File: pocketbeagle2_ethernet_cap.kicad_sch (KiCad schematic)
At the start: 1 part, among them U1 PocketBeagle2

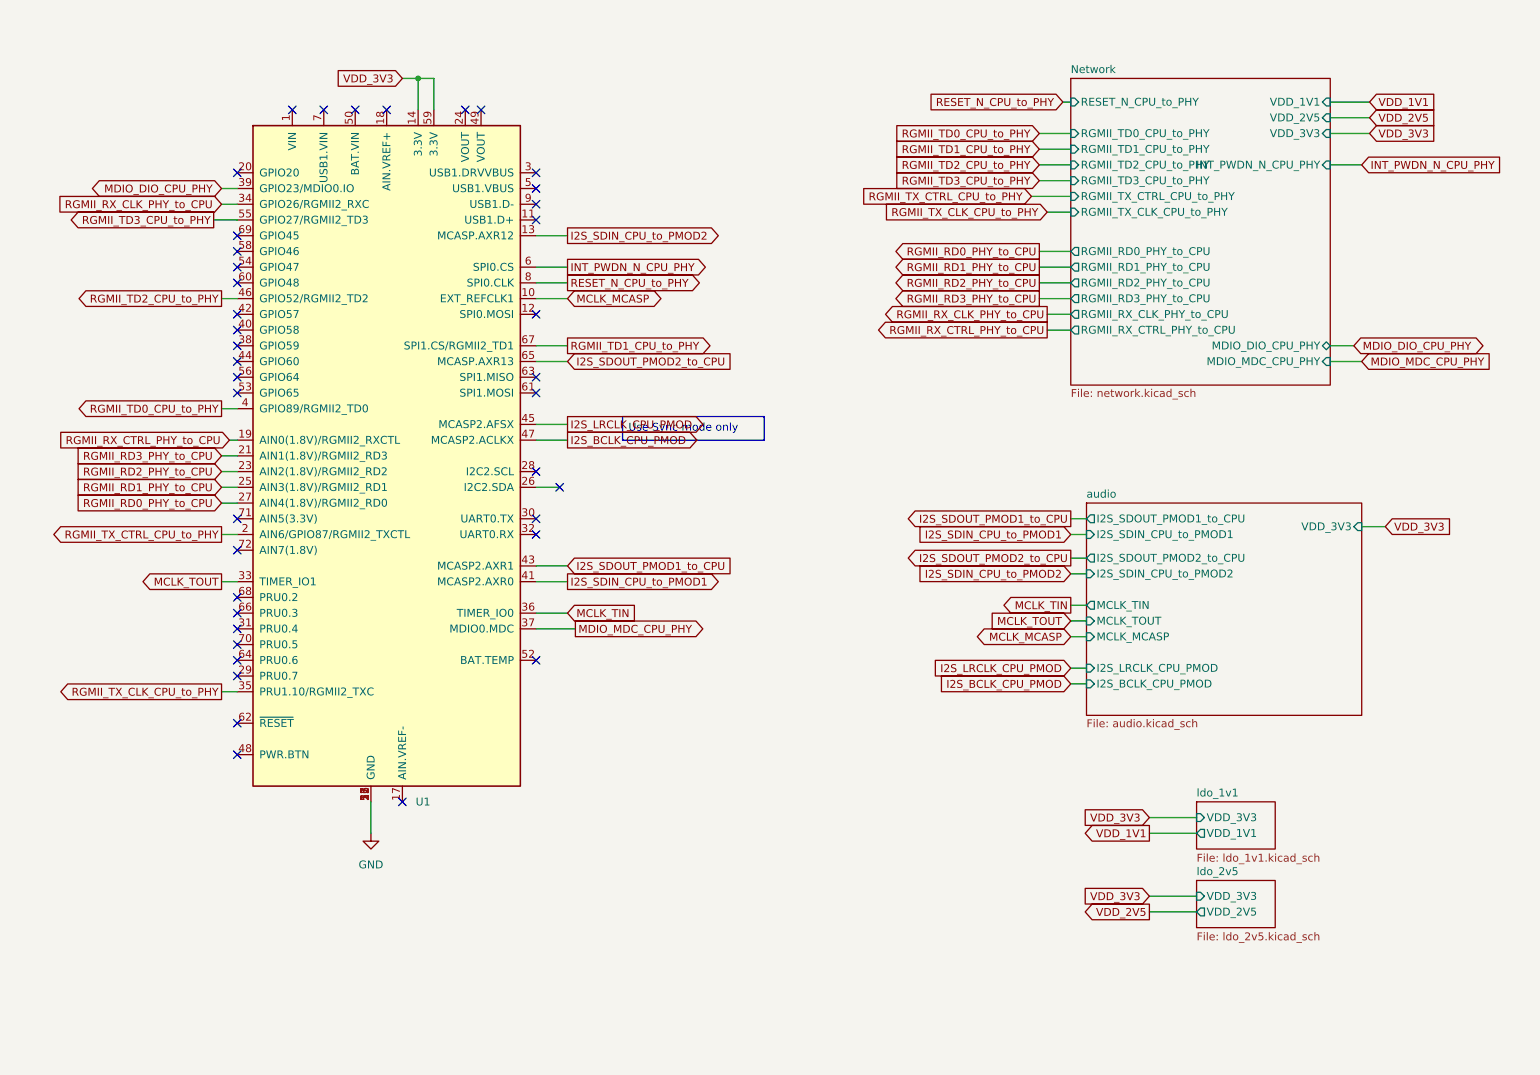
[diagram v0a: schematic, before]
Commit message: Replace audio PMOD sheet with full IO pass-through expansion headers
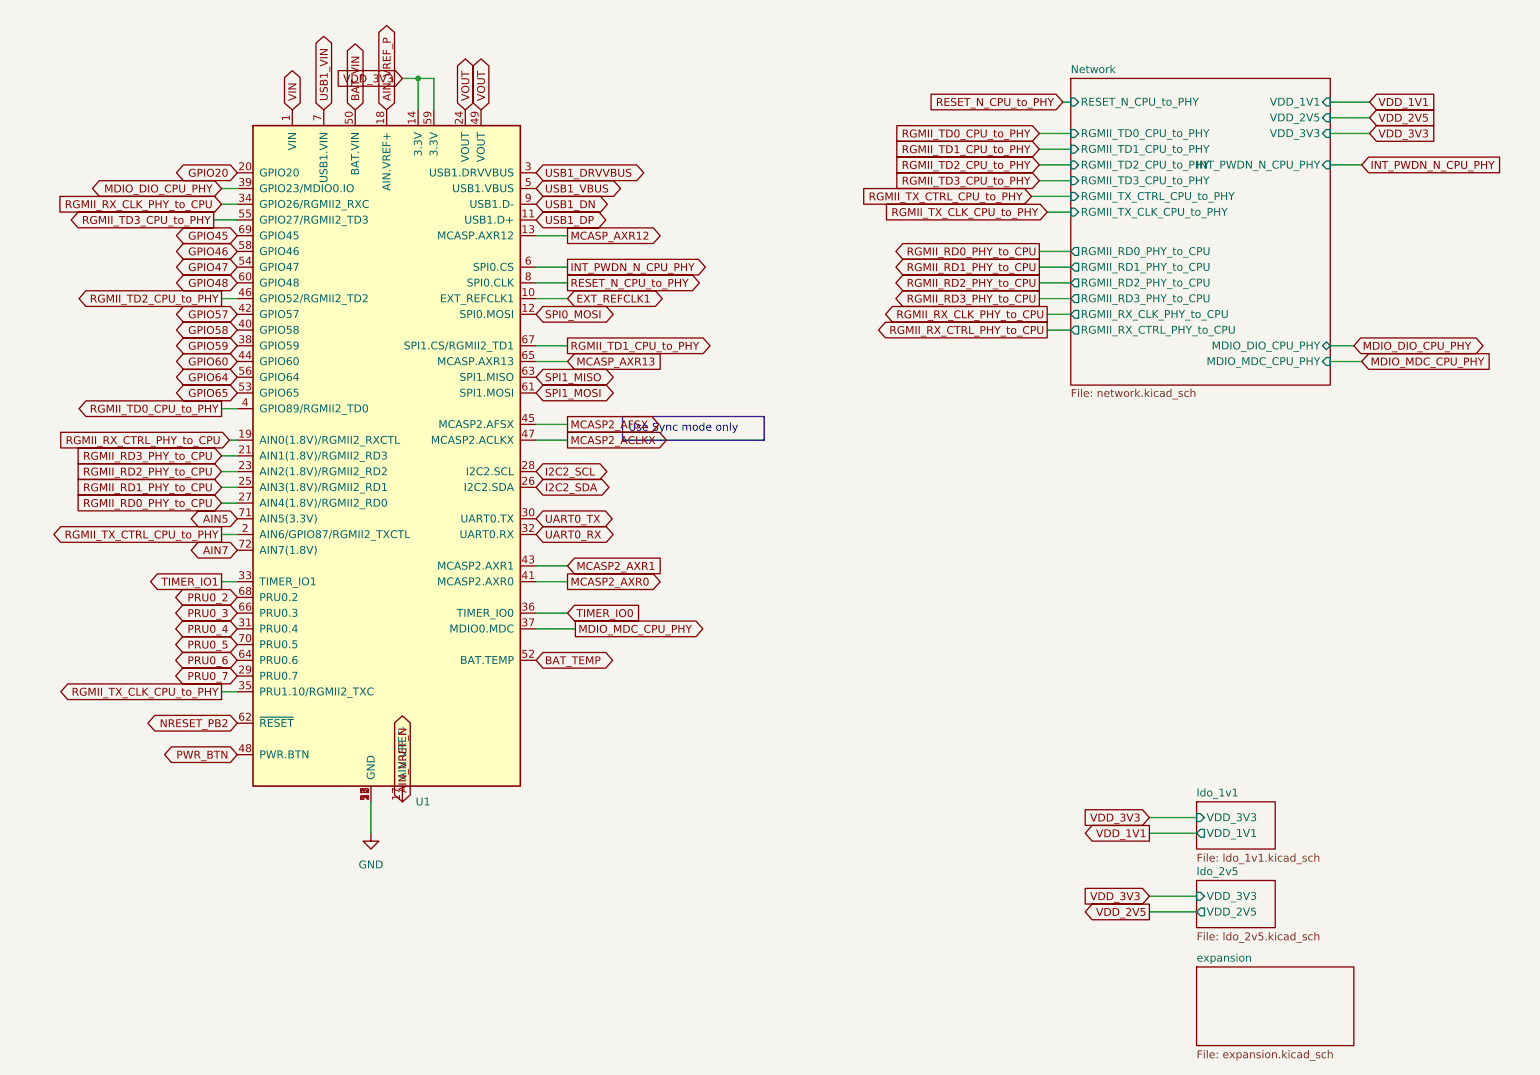
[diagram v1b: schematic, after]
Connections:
- net VIN: now reaches U1.1 (VIN)
- net USB1_DP: now reaches U1.11 (USB1.D+)
- net SPI0_MOSI: now reaches U1.12 (SPI0.MOSI)
- net AIN_VREF_N: now reaches U1.17 (AIN.VREF-)
- net AIN_VREF_P: now reaches U1.18 (AIN.VREF+)
- net GPIO20: now reaches U1.20 (GPIO20)
- net VOUT: now reaches U1.24 (VOUT)
- net VOUT: now also U1.49 (VOUT)
- net I2C2_SDA: now reaches U1.26 (I2C2.SDA)
- net I2C2_SCL: now reaches U1.28 (I2C2.SCL)
- net PRU0_7: now reaches U1.29 (PRU0.7)
- net USB1_DRVVBUS: now reaches U1.3 (USB1.DRVVBUS)
- net UART0_TX: now reaches U1.30 (UART0.TX)
- net PRU0_4: now reaches U1.31 (PRU0.4)
- net UART0_RX: now reaches U1.32 (UART0.RX)
- net GPIO59: now reaches U1.38 (GPIO59)
- net GPIO58: now reaches U1.40 (GPIO58)
- net GPIO57: now reaches U1.42 (GPIO57)
- net GPIO60: now reaches U1.44 (GPIO60)
- net PWR_BTN: now reaches U1.48 (PWR.BTN)
- net USB1_VBUS: now reaches U1.5 (USB1.VBUS)
- net BAT_VIN: now reaches U1.50 (BAT.VIN)
- net BAT_TEMP: now reaches U1.52 (BAT.TEMP)
- net GPIO65: now reaches U1.53 (GPIO65)
- net GPIO47: now reaches U1.54 (GPIO47)
- net GPIO64: now reaches U1.56 (GPIO64)
- net GPIO46: now reaches U1.58 (GPIO46)
- net GPIO48: now reaches U1.60 (GPIO48)
- net SPI1_MOSI: now reaches U1.61 (SPI1.MOSI)
- net NRESET_PB2: now reaches U1.62 (~{RESET})
- net SPI1_MISO: now reaches U1.63 (SPI1.MISO)
- net PRU0_6: now reaches U1.64 (PRU0.6)
- net PRU0_3: now reaches U1.66 (PRU0.3)
- net PRU0_2: now reaches U1.68 (PRU0.2)
- net GPIO45: now reaches U1.69 (GPIO45)
- net USB1_VIN: now reaches U1.7 (USB1.VIN)
- net PRU0_5: now reaches U1.70 (PRU0.5)
- net AIN5: now reaches U1.71 (AIN5(3.3V))
- net AIN7: now reaches U1.72 (AIN7(1.8V))
- net USB1_DN: now reaches U1.9 (USB1.D-)
- net I2S_BCLK_CPU_PMOD renamed MCASP2_ACLKX
- net I2S_LRCLK_CPU_PMOD renamed MCASP2_AFSX
- net I2S_SDIN_CPU_to_PMOD1 renamed MCASP2_AXR0
- net I2S_SDIN_CPU_to_PMOD2 renamed MCASP_AXR12
- net I2S_SDOUT_PMOD1_to_CPU renamed MCASP2_AXR1
- net I2S_SDOUT_PMOD2_to_CPU renamed MCASP_AXR13
- net MCLK_MCASP renamed EXT_REFCLK1
- net MCLK_TIN renamed TIMER_IO0
- net MCLK_TOUT renamed TIMER_IO1
- no-connect marks 40 -> 0
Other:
- removed sheet audio
- added sheet expansion (expansion.kicad_sch)

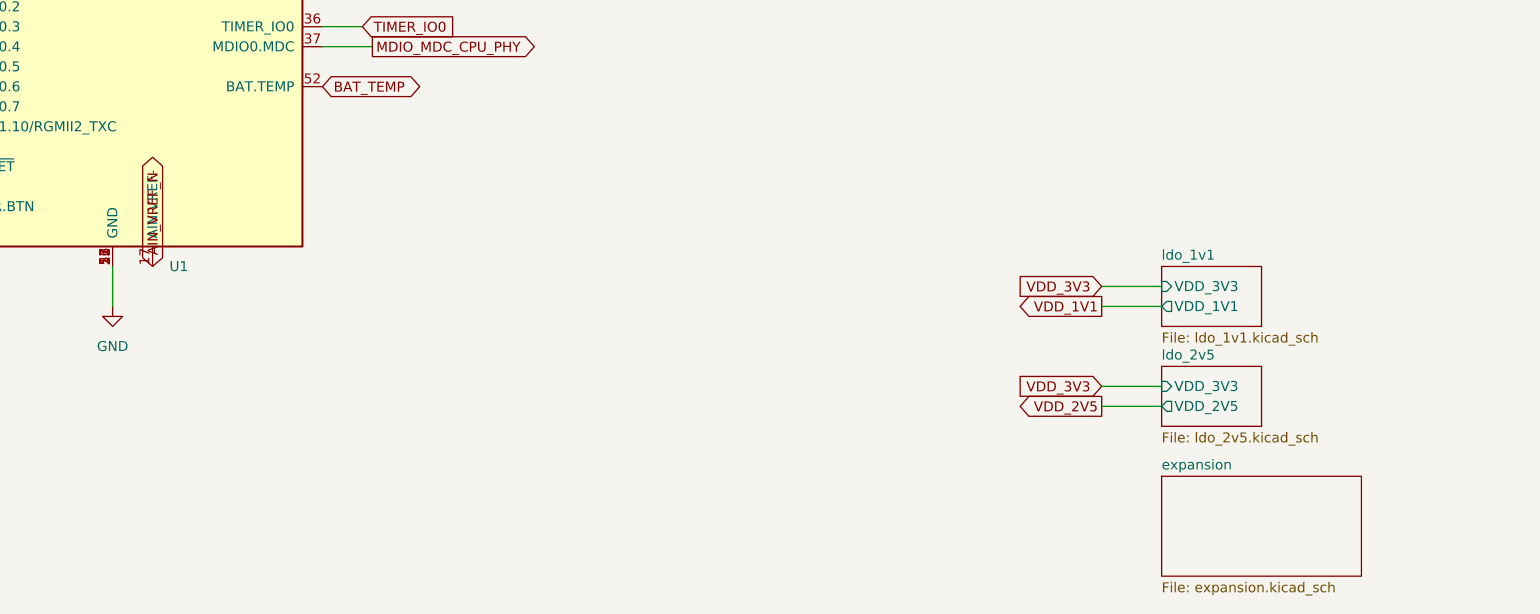
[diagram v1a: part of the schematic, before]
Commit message: Improve schematic readability across all sheets
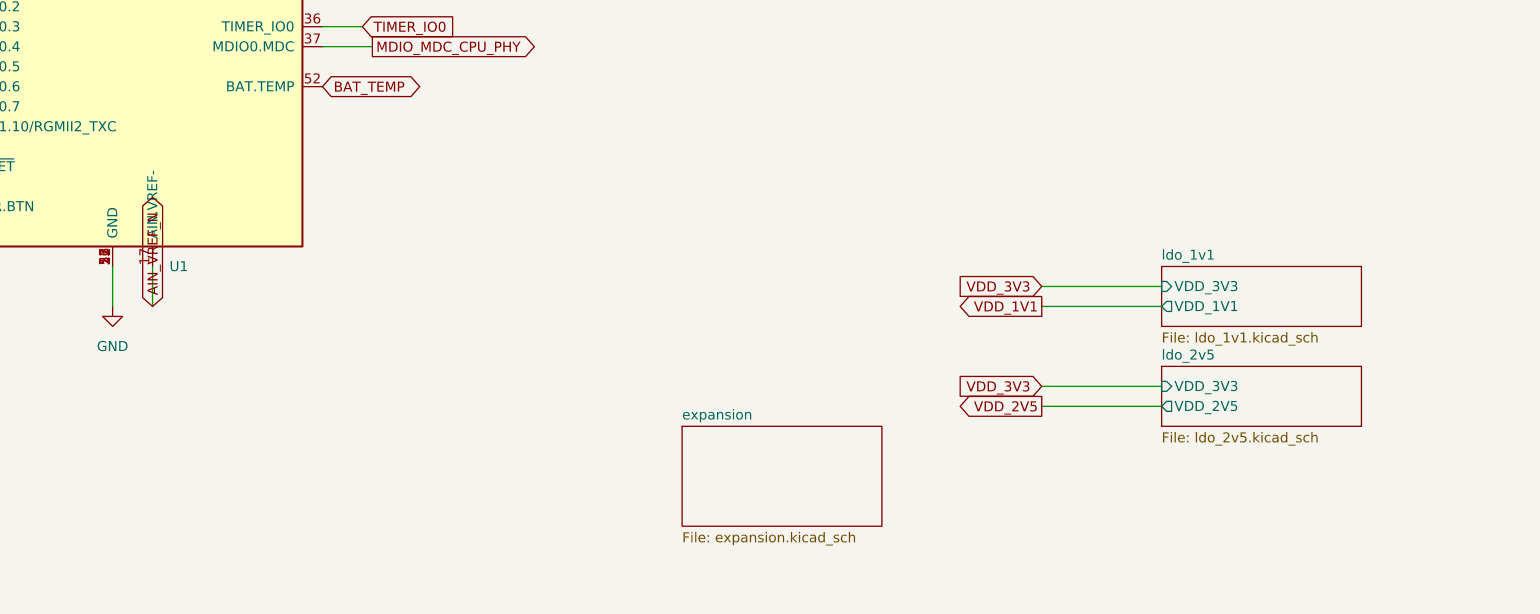
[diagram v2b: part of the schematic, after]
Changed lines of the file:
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@@
 	(sheet
 		(at 198.12 138.43)
-		(size 12.7 7.62)
+		(size 25.4 7.62)
 		(exclude_from_sim no)
 		(in_bom yes)
@@
 	(sheet
 		(at 198.12 151.13)
-		(size 12.7 7.62)
+		(size 25.4 7.62)
 		(exclude_from_sim no)
 		(in_bom yes)
@@
 	(wire
 		(pts
-			(xy 190.5 140.97) (xy 198.12 140.97)
+			(xy 182.88 140.97) (xy 198.12 140.97)
 		)
 		(stroke
@@
 	(global_label "VDD_3V3"
 		(shape input)
-		(at 190.5 140.97 180)
+		(at 182.88 140.97 180)
 		(effects
 			(font
@@
 	(wire
 		(pts
-			(xy 190.5 143.51) (xy 198.12 143.51)
+			(xy 182.88 143.51) (xy 198.12 143.51)
 		)
 		(stroke
@@
 	(global_label "VDD_1V1"
 		(shape output)
-		(at 190.5 143.51 180)
+		(at 182.88 143.51 180)
 		(effects
 			(font
@@
 	(wire
 		(pts
-			(xy 190.5 153.67) (xy 198.12 153.67)
+			(xy 182.88 153.67) (xy 198.12 153.67)
 		)
 		(stroke
@@
 	(global_label "VDD_3V3"
 		(shape input)
-		(at 190.5 153.67 180)
+		(at 182.88 153.67 180)
 		(effects
 			(font
@@
 	(wire
 		(pts
-			(xy 190.5 156.21) (xy 198.12 156.21)
+			(xy 182.88 156.21) (xy 198.12 156.21)
 		)
 		(stroke
@@
 	(global_label "VDD_2V5"
 		(shape output)
-		(at 190.5 156.21 180)
+		(at 182.88 156.21 180)
 		(effects
 			(font
@@
 	(global_label "AIN_VREF_N"
 		(shape bidirectional)
-		(at 69.85 138.43 270)
-		(effects
-			(font
-				(size 1.27 1.27)
-			)
-			(justify left)
+		(at 69.85 143.51 270)
+		(effects
+			(font
+				(size 1.27 1.27)
+			)
+			(justify left)
+		)
+	)
+	(wire
+		(pts
+			(xy 69.85 138.43) (xy 69.85 143.51)
+		)
+		(stroke
+			(width 0)
+			(type default)
 		)
 	)
@@
 	)
 	(sheet
-		(at 198.12 165.1)
+		(at 137.16 158.75)
 		(size 25.4 12.7)
 		(exclude_from_sim no)
@@
 		)
 		(property "Sheetname" "expansion"
-			(at 198.12 164.3884 0)
+			(at 137.16 158.0384 0)
 			(effects
 				(font
@@
 		)
 		(property "Sheetfile" "expansion.kicad_sch"
-			(at 198.12 178.5116 0)
-			(effects
-				(font
+			(at 137.16 172.1616 0)
+			(effects
+				(font
